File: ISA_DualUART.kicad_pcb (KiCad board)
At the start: 2 copper layers, 176.5 x 90.2 mm, 75 parts, among them J1 ISA BUS, J10 Parallel Port, J2 ADDR_IRQ, J3 UART1_SEL, J4 UART2_SEL, J6 Serial 2 IDC, J7 Serial 1 DB9, J9 Parport IRQ Select, U1 74LS138, U11 74LS30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

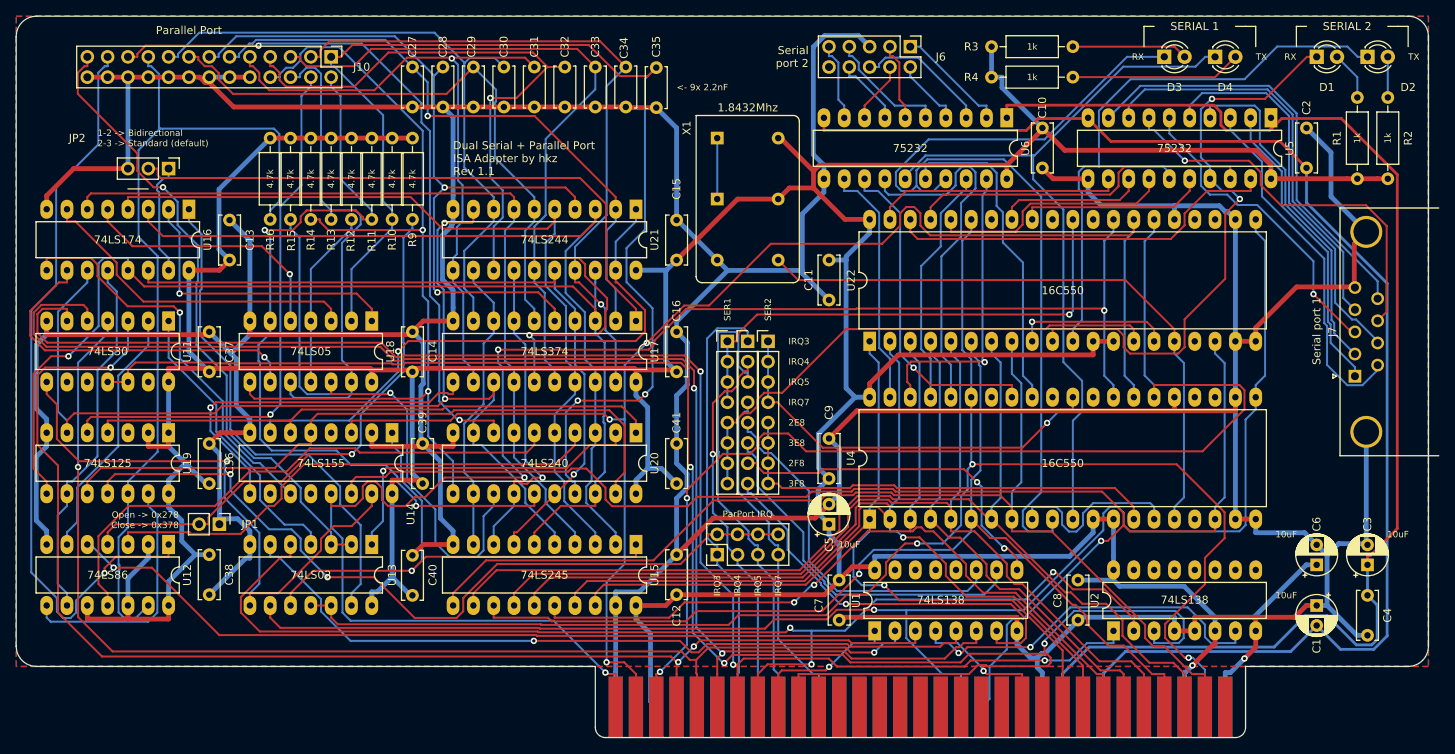
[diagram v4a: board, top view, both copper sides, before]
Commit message: Reworked the board, added LED indicators for parport
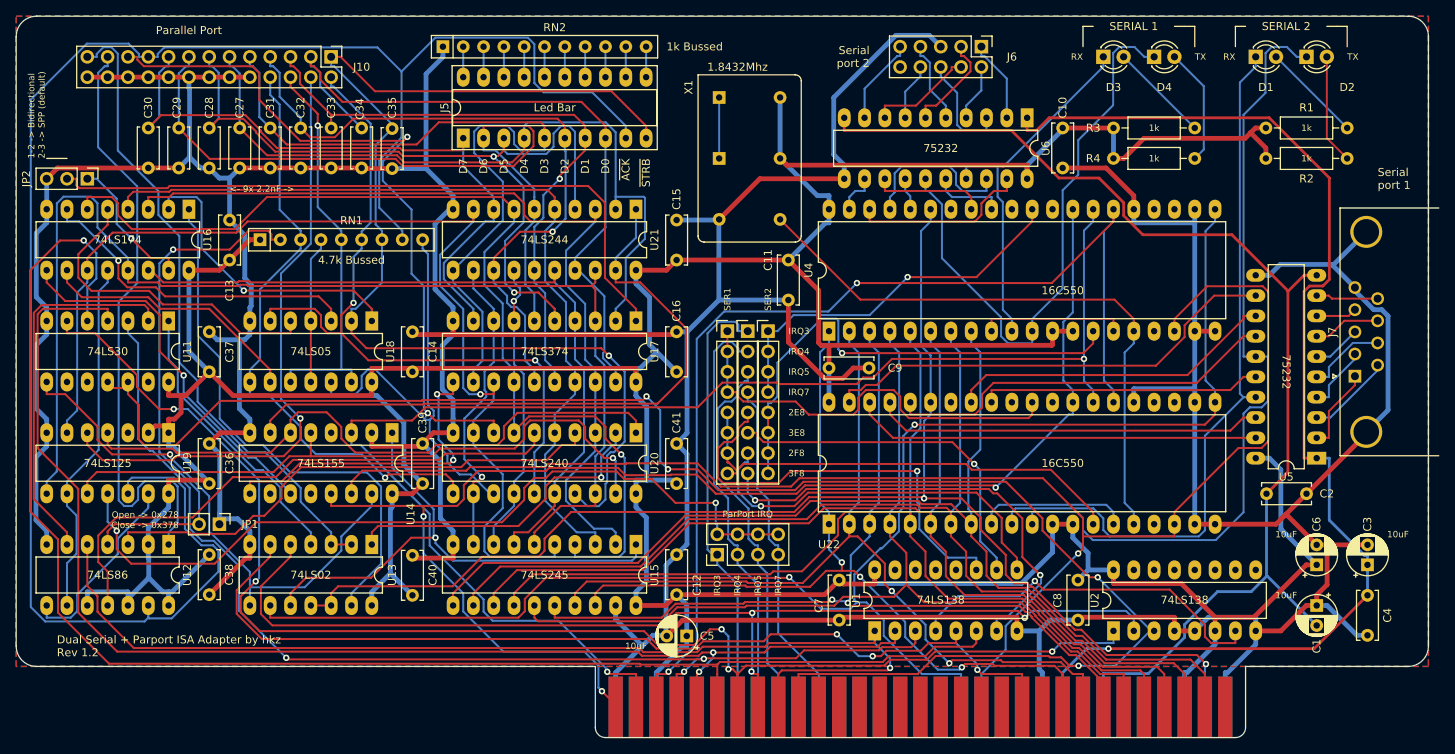
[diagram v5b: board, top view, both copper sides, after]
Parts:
- removed R10, R11, R12, R13, R14, R15, R16, R9: 4.7k, Resistor_THT:R_Axial_DIN0207_L6.3mm_D2.5mm_P10.16mm_Horizontal
- added J5: Parallel Port LEDs, Package_DIP:DIP-20_W7.62mm_Socket_LongPads, F.Cu at (194.3, 128.3)
- added RN1: 4.7k, Resistor_THT:R_Array_SIP9, F.Cu at (168.9, 141.0)
- added RN2: 1k, Resistor_THT:R_Array_SIP11, F.Cu at (191.8, 116.8)
- moved C2 45.7 mm to (299.7, 172.7), turned to 180 degrees
- moved C30 45.1 mm to (154.9, 127.0)
- moved U5 42.9 mm to (301.0, 168.3), turned to 180 degrees
- moved C29 37.6 mm to (158.8, 127.0)
- moved C35 33.9 mm to (185.4, 132.1)
- moved C31 33.9 mm to (170.2, 127.0)
- moved C32 33.9 mm to (174.0, 127.0)
- moved C33 33.9 mm to (177.8, 127.0)
- moved C34 33.9 mm to (181.6, 127.0)
- moved C28 30.2 mm to (162.6, 127.0)
- moved U4 24.0 mm to (240.0, 152.4)
- moved U22 23.4 mm to (240.0, 176.5)
- moved C27 22.9 mm to (166.4, 127.0)
- moved C5 22.6 mm to (222.2, 190.5), turned to 180 degrees
- moved R3 18.3 mm to (285.8, 127.0)
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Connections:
- net /~PARPORT_ACK renamed /RN_7
- net /~PARPORT_AUTOFD renamed /RN_5
- net /~PARPORT_INIT renamed /RN_4
- net /~PARPORT_SLCTIN renamed /RN_2
- net /~PARPORT_STROBE renamed /RN_6
- net Net-(JP1-Pad2) renamed /RN_1
- net Net-(R12-Pad2) renamed /RN_3
- net Net-(R15-Pad2) renamed /RN_8
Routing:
- net /RN_7: track 105.5 -> 228.4 mm
- net /SIN_2: track 116.6 -> 46.4 mm
- net VCC: track 626.5 -> 574.9 mm, vias 1 -> 0
- net /RS232_1_DTR: track 51.8 -> 5.10 mm
- net /RS232_1_RI: track 54.0 -> 7.78 mm
- net GND: track 798.9 -> 754.8 mm, vias 1 -> 0
- net /~CTS_2: track 46.1 -> 4.07 mm
- net /RS232_1_CTS: track 49.5 -> 8.42 mm, vias 1 -> 0
- net /RS232_1_RTS: track 49.0 -> 10.1 mm
- net /A0: track 207.1 -> 170.6 mm, vias 4 -> 3
- net /RN_2: track 111.7 -> 76.5 mm, vias 2 -> 1
- net /RS232_1_RX: track 43.4 -> 8.27 mm
- net /RS232_1_DSR: track 44.7 -> 10.7 mm
- net /RS232_1_TX: track 39.3 -> 6.06 mm, vias 1 -> 0
- net /~RTS_2: track 41.0 -> 9.08 mm
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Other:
- board text added: "1-2 -> Bidirectional 2-3 -> SPP (default)"
- board text added: "1k Bussed"
- board text added: "4.7k Bussed"
- board text added: "<- 9x 2.2nF ->"
- board text added: "D0"
- board text added: "D1"
- board text added: "D2"
- board text added: "D3"
- board text added: "D4"
- board text added: "D5"
- board text added: "D6"
- board text added: "D7"
- board text added: "Dual Serial + Parport ISA Adapter by hkz Rev 1.2"
- board text added: "Led Bar"
- board text added: "~ACK"
- board text added: "~STRB"
- board text removed: "1-2 -> Bidirectional 2-3 -> Standard (default)"
- board text removed: "4.7k"
- board text removed: "<- 9x 2.2nF"
- board text removed: "Dual Serial + Parallel Port ISA Adapter by hkz Rev 1.1"
